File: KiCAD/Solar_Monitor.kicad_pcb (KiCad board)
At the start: 2 copper layers, 40.6 x 22.9 mm, 16 parts, among them J1 Power IN, J2 Power Out, Q1 PN2222A, Q2 MCP102-300E/TO, SW1 SW_Push, U1 PIC16F15214-I/P

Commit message: minor update to pcb
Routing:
- net Net-(C1-Pad2): track 36.5 -> 33.5 mm
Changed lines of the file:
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@@
   (segment (start 111.3536 80.0608) (end 111.3536 79.3124) (width 0.25) (layer "F.Cu") (net 2))
   (segment (start 92.72 68.68) (end 98.144 68.68) (width 0.25) (layer "F.Cu") (net 3))
+  (segment (start 88.9 73.66) (end 86.36 71.12) (width 0.25) (layer "F.Cu") (net 3))
   (segment (start 92.72 68.68) (end 92.72 65.2264) (width 0.25) (layer "F.Cu") (net 3))
-  (segment (start 88.9 72.5) (end 88.9 76.2) (width 0.25) (layer "F.Cu") (net 3))
-  (segment (start 92.72 68.68) (end 91.67 68.68) (width 0.25) (layer "F.Cu") (net 3))
+  (segment (start 88.9 76.2) (end 88.9 73.66) (width 0.25) (layer "F.Cu") (net 3))
+  (segment (start 92.72 68.68) (end 90.28 71.12) (width 0.25) (layer "F.Cu") (net 3))
   (segment (start 99.4664 70.0024) (end 105.843776 70.0024) (width 0.25) (layer "F.Cu") (net 3))
+  (segment (start 90.28 71.12) (end 86.36 71.12) (width 0.25) (layer "F.Cu") (net 3))
   (segment (start 98.144 68.68) (end 99.4664 70.0024) (width 0.25) (layer "F.Cu") (net 3))
-  (segment (start 91.67 68.68) (end 88.9 71.45) (width 0.25) (layer "F.Cu") (net 3))
   (segment (start 105.843776 70.0024) (end 106.6292 70.787824) (width 0.25) (layer "F.Cu") (net 3))
-  (segment (start 86.36 71.12) (end 87.52 71.12) (width 0.25) (layer "F.Cu") (net 3))
-  (segment (start 88.9 71.45) (end 88.9 76.2) (width 0.25) (layer "F.Cu") (net 3))
   (segment (start 106.6292 70.787824) (end 106.6292 72.5468) (width 0.25) (layer "F.Cu") (net 3))
-  (segment (start 87.52 71.12) (end 88.9 72.5) (width 0.25) (layer "F.Cu") (net 3))
   (segment (start 104.0892 72.5468) (end 105.4056 73.8632) (width 0.25) (layer "F.Cu") (net 8))
   (segment (start 107.95 73.1012) (end 107.95 68.1228) (width 0.25) (layer "F.Cu") (net 8))

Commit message: Rebuild Gerber files
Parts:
- added REF**: OSHW-Logo2_7.3x6mm_SilkScreen, Symbol:OSHW-Logo2_7.3x6mm_SilkScreen, B.Cu at (182.2, 83.0)
- moved J2 86.8 mm to (202.5, 87.1)
- moved REF1 86.8 mm to (168.6, 82.1)
- moved REF2 86.8 mm to (204.1, 82.1)
- moved REF4 86.8 mm to (204.1, 99.9)
- moved TP1 86.8 mm to (181.2, 98.6)
- moved TP2 86.8 mm to (196.1, 98.6)
- moved C1 86.8 mm to (172.6, 83.7)
- moved D1 86.8 mm to (199.4, 85.7)
- moved J1 86.8 mm to (171.1, 89.7)
- moved U1 86.8 mm to (177.5, 87.3)
- moved Q1 86.8 mm to (188.9, 91.1)
- moved Q2 86.8 mm to (188.9, 97.4)
- moved REF3 86.8 mm to (168.6, 99.9)
- moved RV1 86.8 mm to (173.7, 94.8)
- moved SW1 86.8 mm to (198.9, 88.6)
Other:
- board text added: "https://github.com/mattrude/solar-monitor"

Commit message: Moving on
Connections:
- net Net-(C1-Pad1) renamed /-5v
- net Net-(C1-Pad2) renamed /+5v

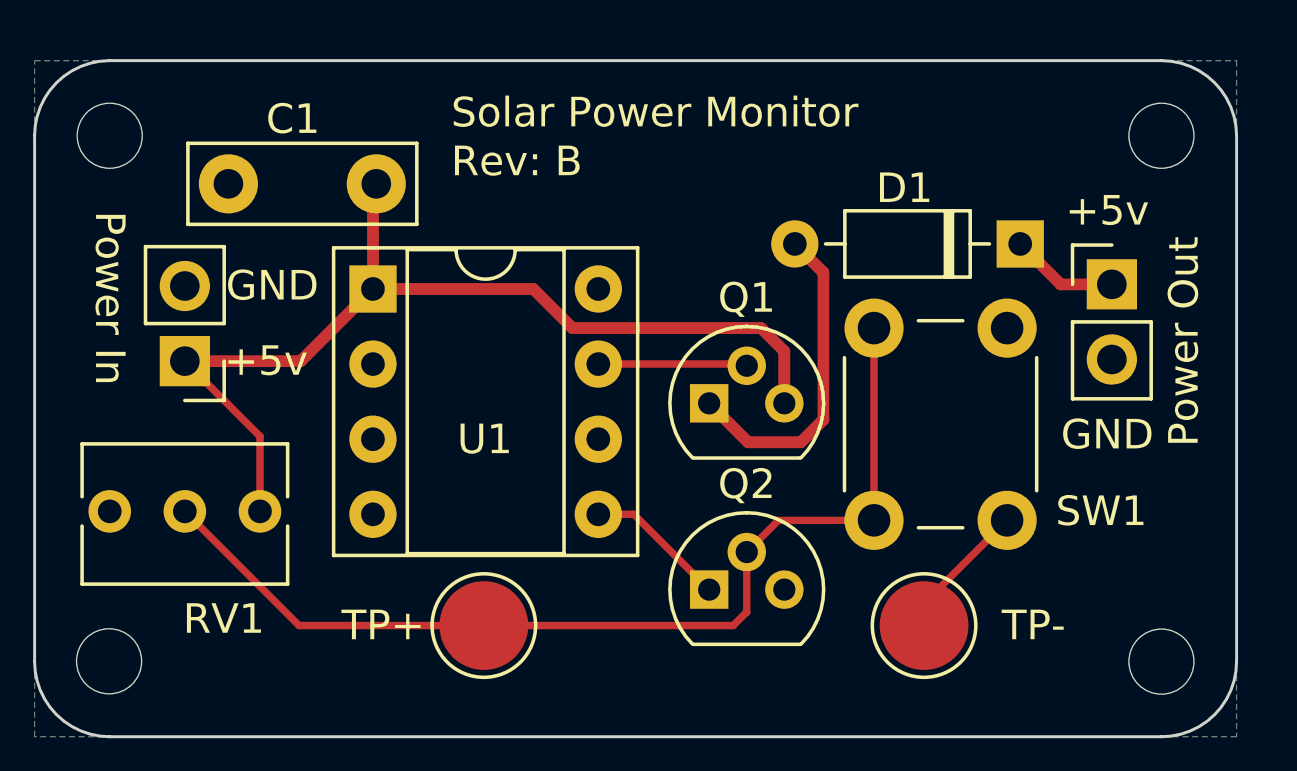
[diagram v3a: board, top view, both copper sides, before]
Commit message: Switch to an ATTiny402
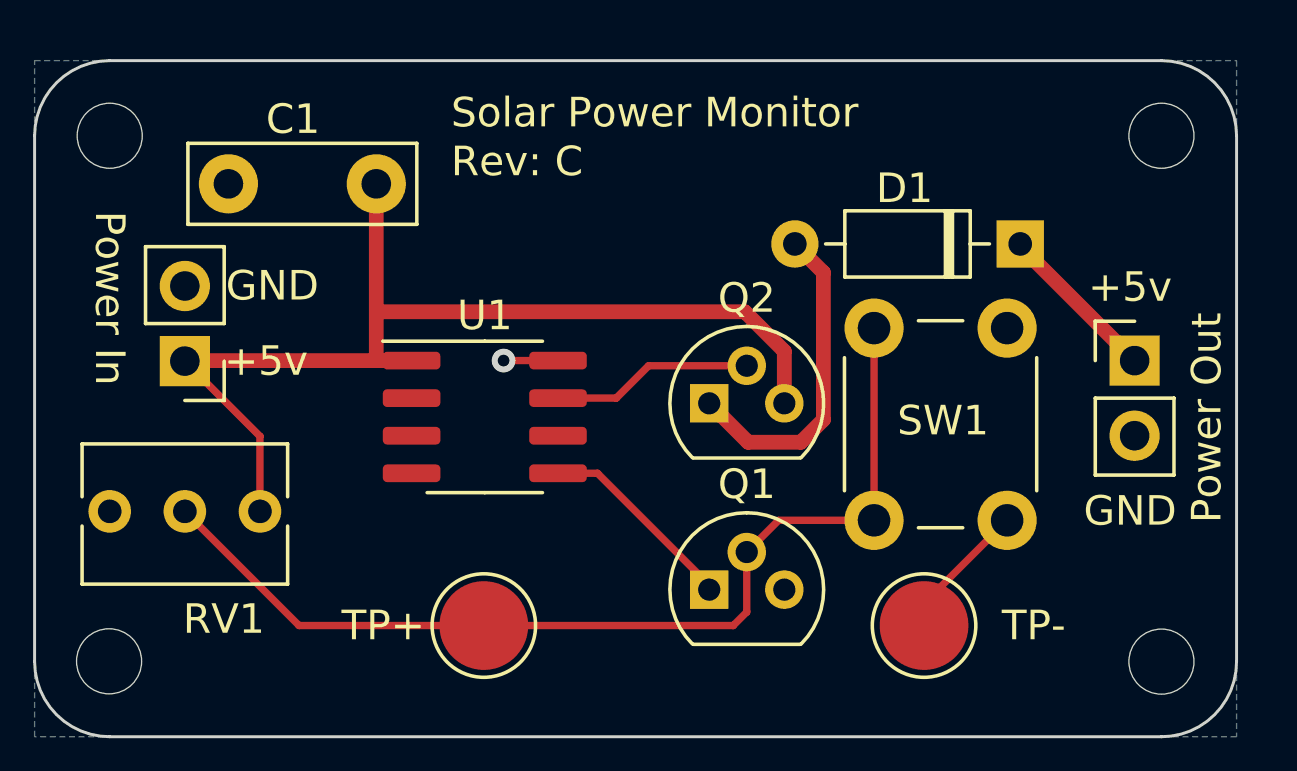
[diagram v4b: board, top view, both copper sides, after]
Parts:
- Q1: renamed from Q2; value MCP102-300E/TO -> MCP102-300E
- U1: footprint Package_DIP:DIP-8_W7.62mm_Socket -> Package_SO:SOIC-8_3.9x4.9mm_P1.27mm
- moved U1 5.75 mm to (181.3, 91.6)
- moved J2 2.69 mm to (203.2, 89.7)
- renumbered Q1 to Q2
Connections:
- net /-5v renamed /GND
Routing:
- net /+5v: track 33.5 -> 35.8 mm
- net Net-(Q2-Pad2): track 5.15 -> 7.28 mm
- net Net-(Q1-Pad1): track 4.80 -> 6.83 mm
- net Net-(D1-Pad1): track 3.66 -> 5.55 mm
- net /GND: track 4.72 -> 6.56 mm, vias 0 -> 1
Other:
- board text added: "Rev: C"
